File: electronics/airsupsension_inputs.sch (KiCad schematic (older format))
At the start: 46 parts, among them U6 LM324ID, U7 LM324ID

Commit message: more footprints...
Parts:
- C10: value 220nF -> 220n; footprint (none) -> Capacitors_SMD:C_0805; farnell (none) -> 1288261; name (none) -> C0805C224K5RACTU
- C11, C12, C13, C14, C15, C16, C7, C8: footprint (none) -> Capacitors_SMD:C_0805; farnell (none) -> 2118131; name (none) -> C0805C105K5RACTU
- C9: footprint (none) -> Capacitors_SMD:C_0805; farnell (none) -> 1288261; name (none) -> C0805C224K5RACTU
- F1, F2, F3, F4, F5, F6, F7, F8: footprint (none) -> Resistors_SMD:R_1210; farnell (none) -> 1345917; name (none) -> MICROSMD010F-2
- R27, R28, R33, R34, R39, R41, R47, R48: footprint (none) -> Resistors_SMD:R_0805; farnell (none) -> 612522; name (none) -> CR0805-FX-1002ELF
- R29, R31, R35, R37, R42, R44, R49, R51: footprint (none) -> Resistors_SMD:R_0805; farnell (none) -> 2117129; name (none) -> RP73PF2A499RBTDF
- R30, R32, R36, R38, R43, R45, R50, R52: footprint (none) -> Resistors_SMD:R_0805; farnell (none) -> 1577659; name (none) -> ERA6AEB102V
- R40, R46: footprint (none) -> Resistors_SMD:R_0805; farnell (none) -> 1575826; name (none) -> MCTC0525B2001T5E
- U6, U7: value LM324ID -> LM224; footprint (none) -> SMD_Packages:SOIC-14_N; farnell (none) -> 1426352; name (none) -> LM224DR2G
- U6, U7: value LM324ID -> LM224
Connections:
- wire segments 89 -> 88

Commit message: Firmware and some changes in electronics schema
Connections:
- wire segments 88 -> 92
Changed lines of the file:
@@
 $EndComp
 $Comp
-L GND #PWR25
+L GND #PWR022
 U 1 1 5505A367
 P 2450 2750
-F 0 "#PWR25" H 2450 2500 60  0001 C CNN
+F 0 "#PWR022" H 2450 2500 60  0001 C CNN
 F 1 "GND" H 2450 2600 60  0000 C CNN
 F 2 "" H 2450 2750 60  0000 C CNN
@@
 $EndComp
 $Comp
-L GND #PWR21
+L GND #PWR023
 U 1 1 5505A385
 P 1650 2150
-F 0 "#PWR21" H 1650 1900 60  0001 C CNN
+F 0 "#PWR023" H 1650 1900 60  0001 C CNN
 F 1 "GND" H 1650 2000 60  0000 C CNN
 F 2 "" H 1650 2150 60  0000 C CNN
@@
 $EndComp
 $Comp
-L GND #PWR19
+L GND #PWR024
 U 1 1 5505A3C1
 P 1050 2050
-F 0 "#PWR19" H 1050 1800 60  0001 C CNN
+F 0 "#PWR024" H 1050 1800 60  0001 C CNN
 F 1 "GND" H 1050 1900 60  0000 C CNN
 F 2 "" H 1050 2050 60  0000 C CNN
@@
 $EndComp
 $Comp
-L GND #PWR23
+L GND #PWR025
 U 1 1 5505A61E
 P 2150 1350
-F 0 "#PWR23" H 2150 1100 60  0001 C CNN
+F 0 "#PWR025" H 2150 1100 60  0001 C CNN
 F 1 "GND" H 2150 1200 60  0000 C CNN
 F 2 "" H 2150 1350 60  0000 C CNN
@@
 $EndComp
 $Comp
-L GND #PWR26
+L GND #PWR026
 U 1 1 5505C0F9
 P 2550 5750
-F 0 "#PWR26" H 2550 5500 60  0001 C CNN
+F 0 "#PWR026" H 2550 5500 60  0001 C CNN
 F 1 "GND" H 2550 5600 60  0000 C CNN
 F 2 "" H 2550 5750 60  0000 C CNN
@@
 $EndComp
 $Comp
-L GND #PWR22
+L GND #PWR027
 U 1 1 5505C0FF
 P 1750 5150
-F 0 "#PWR22" H 1750 4900 60  0001 C CNN
+F 0 "#PWR027" H 1750 4900 60  0001 C CNN
 F 1 "GND" H 1750 5000 60  0000 C CNN
 F 2 "" H 1750 5150 60  0000 C CNN
@@
 $EndComp
 $Comp
-L GND #PWR20
+L GND #PWR028
 U 1 1 5505C105
 P 1150 5050
-F 0 "#PWR20" H 1150 4800 60  0001 C CNN
+F 0 "#PWR028" H 1150 4800 60  0001 C CNN
 F 1 "GND" H 1150 4900 60  0000 C CNN
 F 2 "" H 1150 5050 60  0000 C CNN
@@
 $EndComp
 $Comp
-L GND #PWR31
+L GND #PWR029
 U 1 1 5505C836
 P 4800 2700
-F 0 "#PWR31" H 4800 2450 60  0001 C CNN
+F 0 "#PWR029" H 4800 2450 60  0001 C CNN
 F 1 "GND" H 4800 2550 60  0000 C CNN
 F 2 "" H 4800 2700 60  0000 C CNN
@@
 $EndComp
 $Comp
-L GND #PWR29
+L GND #PWR030
 U 1 1 5505C83C
 P 4000 2100
-F 0 "#PWR29" H 4000 1850 60  0001 C CNN
+F 0 "#PWR030" H 4000 1850 60  0001 C CNN
 F 1 "GND" H 4000 1950 60  0000 C CNN
 F 2 "" H 4000 2100 60  0000 C CNN
@@
 $EndComp
 $Comp
-L GND #PWR27
+L GND #PWR031
 U 1 1 5505C842
 P 3400 2000
-F 0 "#PWR27" H 3400 1750 60  0001 C CNN
+F 0 "#PWR031" H 3400 1750 60  0001 C CNN
 F 1 "GND" H 3400 1850 60  0000 C CNN
 F 2 "" H 3400 2000 60  0000 C CNN
@@
 $EndComp
 $Comp
-L GND #PWR38
+L GND #PWR032
 U 1 1 5505CD91
 P 7250 2700
-F 0 "#PWR38" H 7250 2450 60  0001 C CNN
+F 0 "#PWR032" H 7250 2450 60  0001 C CNN
 F 1 "GND" H 7250 2550 60  0000 C CNN
 F 2 "" H 7250 2700 60  0000 C CNN
@@
 $EndComp
 $Comp
-L GND #PWR35
+L GND #PWR033
 U 1 1 5505CD97
 P 6450 2100
-F 0 "#PWR35" H 6450 1850 60  0001 C CNN
+F 0 "#PWR033" H 6450 1850 60  0001 C CNN
 F 1 "GND" H 6450 1950 60  0000 C CNN
 F 2 "" H 6450 2100 60  0000 C CNN
@@
 $EndComp
 $Comp
-L GND #PWR33
+L GND #PWR034
 U 1 1 5505CD9D
 P 5850 2000
-F 0 "#PWR33" H 5850 1750 60  0001 C CNN
+F 0 "#PWR034" H 5850 1750 60  0001 C CNN
 F 1 "GND" H 5850 1850 60  0000 C CNN
 F 2 "" H 5850 2000 60  0000 C CNN
@@
 $EndComp
 $Comp
-L GND #PWR44
+L GND #PWR035
 U 1 1 5505D503
 P 10200 2800
-F 0 "#PWR44" H 10200 2550 60  0001 C CNN
+F 0 "#PWR035" H 10200 2550 60  0001 C CNN
 F 1 "GND" H 10200 2650 60  0000 C CNN
 F 2 "" H 10200 2800 60  0000 C CNN
@@
 $EndComp
 $Comp
-L GND #PWR42
+L GND #PWR036
 U 1 1 5505D509
 P 9400 2200
-F 0 "#PWR42" H 9400 1950 60  0001 C CNN
+F 0 "#PWR036" H 9400 1950 60  0001 C CNN
 F 1 "GND" H 9400 2050 60  0000 C CNN
 F 2 "" H 9400 2200 60  0000 C CNN
@@
 $EndComp
 $Comp
-L GND #PWR41
+L GND #PWR037
 U 1 1 5505D50F
 P 8800 2100
-F 0 "#PWR41" H 8800 1850 60  0001 C CNN
+F 0 "#PWR037" H 8800 1850 60  0001 C CNN
 F 1 "GND" H 8800 1950 60  0000 C CNN
 F 2 "" H 8800 2100 60  0000 C CNN
@@
 $EndComp
 $Comp
-L GND #PWR32
+L GND #PWR038
 U 1 1 5505D6E9
 P 5050 5750
-F 0 "#PWR32" H 5050 5500 60  0001 C CNN
+F 0 "#PWR038" H 5050 5500 60  0001 C CNN
 F 1 "GND" H 5050 5600 60  0000 C CNN
 F 2 "" H 5050 5750 60  0000 C CNN
@@
 $EndComp
 $Comp
-L GND #PWR30
+L GND #PWR039
 U 1 1 5505D6EF
 P 4250 5150
-F 0 "#PWR30" H 4250 4900 60  0001 C CNN
+F 0 "#PWR039" H 4250 4900 60  0001 C CNN
 F 1 "GND" H 4250 5000 60  0000 C CNN
 F 2 "" H 4250 5150 60  0000 C CNN
@@
 $EndComp
 $Comp
-L GND #PWR28
+L GND #PWR040
 U 1 1 5505D6F5
 P 3650 5050
-F 0 "#PWR28" H 3650 4800 60  0001 C CNN
+F 0 "#PWR040" H 3650 4800 60  0001 C CNN
 F 1 "GND" H 3650 4900 60  0000 C CNN
 F 2 "" H 3650 5050 60  0000 C CNN
@@
 $EndComp
 $Comp
-L GND #PWR39
+L GND #PWR041
 U 1 1 5505D87C
 P 7600 5850
-F 0 "#PWR39" H 7600 5600 60  0001 C CNN
+F 0 "#PWR041" H 7600 5600 60  0001 C CNN
 F 1 "GND" H 7600 5700 60  0000 C CNN
 F 2 "" H 7600 5850 60  0000 C CNN
@@
 $EndComp
 $Comp
-L GND #PWR36
+L GND #PWR042
 U 1 1 5505D882
 P 6800 5250
-F 0 "#PWR36" H 6800 5000 60  0001 C CNN
+F 0 "#PWR042" H 6800 5000 60  0001 C CNN
 F 1 "GND" H 6800 5100 60  0000 C CNN
 F 2 "" H 6800 5250 60  0000 C CNN
@@
 $EndComp
 $Comp
-L GND #PWR34
+L GND #PWR043
 U 1 1 5505D888
 P 5950 5250
-F 0 "#PWR34" H 5950 5000 60  0001 C CNN
+F 0 "#PWR043" H 5950 5000 60  0001 C CNN
 F 1 "GND" H 5950 5100 60  0000 C CNN
 F 2 "" H 5950 5250 60  0000 C CNN
@@
 Wire Wire Line
 	6400 5550 6400 4950
-Wire Wire Line
-	5950 4750 6400 4750
 Text GLabel 6800 4250 2    60   Input ~ 0
 +5V
@@
 	1    0    0    -1
 $EndComp
-Connection ~ 6200 4750
 Wire Wire Line
 	6200 5150 6200 5250
@@
 $EndComp
 $Comp
-L GND #PWR45
+L GND #PWR044
 U 1 1 5505E94C
 P 10250 5700
-F 0 "#PWR45" H 10250 5450 60  0001 C CNN
+F 0 "#PWR044" H 10250 5450 60  0001 C CNN
 F 1 "GND" H 10250 5550 60  0000 C CNN
 F 2 "" H 10250 5700 60  0000 C CNN
@@
 $EndComp
 $Comp
-L GND #PWR43
+L GND #PWR045
 U 1 1 5505E952
 P 9450 5100
-F 0 "#PWR43" H 9450 4850 60  0001 C CNN
+F 0 "#PWR045" H 9450 4850 60  0001 C CNN
 F 1 "GND" H 9450 4950 60  0000 C CNN
 F 2 "" H 9450 5100 60  0000 C CNN
@@
 $EndComp
 $Comp
-L GND #PWR40
+L GND #PWR046
 U 1 1 5505E958
 P 8600 5100
-F 0 "#PWR40" H 8600 4850 60  0001 C CNN
+F 0 "#PWR046" H 8600 4850 60  0001 C CNN
 F 1 "GND" H 8600 4950 60  0000 C CNN
 F 2 "" H 8600 5100 60  0000 C CNN
@@
 Wire Wire Line
 	9050 5400 9050 4800
-Wire Wire Line
-	8600 4600 9050 4600
 Text GLabel 9450 4100 2    60   Input ~ 0
 +5V
@@
 $EndComp
 $Comp
-L GND #PWR37
+L GND #PWR047
 U 1 1 5511D5C7
 P 6900 1300
-F 0 "#PWR37" H 6900 1050 60  0001 C CNN
+F 0 "#PWR047" H 6900 1050 60  0001 C CNN
 F 1 "GND" H 6900 1150 60  0000 C CNN
 F 2 "" H 6900 1300 60  0000 C CNN
@@
 Wire Wire Line
 	6900 1250 6900 1300
+Wire Wire Line
+	6400 4750 6200 4750
+Wire Wire Line
+	6200 4250 5950 4250
+Wire Wire Line
+	5950 4250 5950 4750
+Wire Wire Line
+	8850 4600 9050 4600
+Wire Wire Line
+	8850 4100 8600 4100
+Wire Wire Line
+	8600 4100 8600 4600
 $EndSCHEMATC

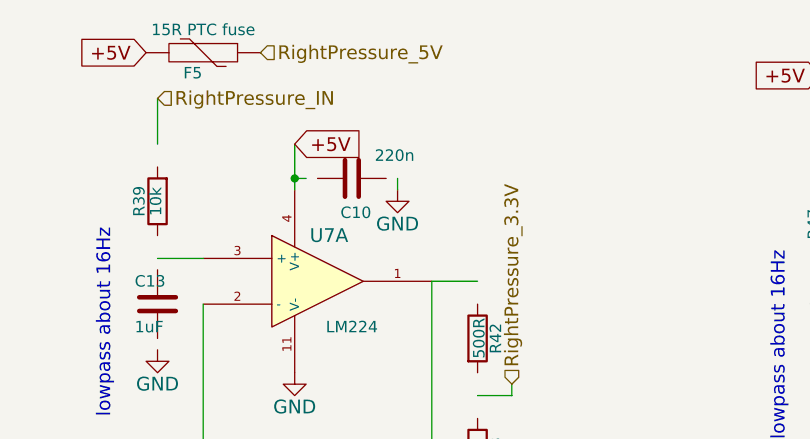
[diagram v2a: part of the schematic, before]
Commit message: Some more footprints and beginning PCB work
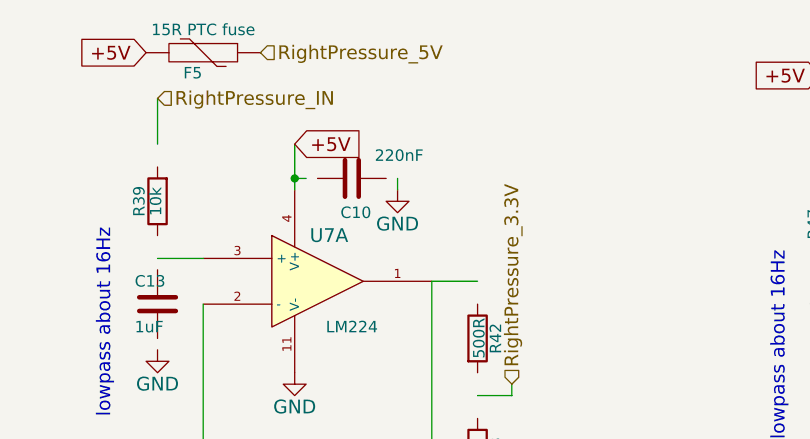
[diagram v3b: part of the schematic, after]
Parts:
- C10: value 220n -> 220nF
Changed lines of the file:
@@
 P 6700 1250
 F 0 "C10" V 6850 1200 50  0000 L CNN
-F 1 "220n" V 6600 1350 50  0000 L CNN
+F 1 "220nF" V 6600 1350 50  0000 L CNN
 F 2 "Capacitors_SMD:C_0805" H 6738 1100 30  0001 C CNN
 F 3 "" H 6700 1250 60  0000 C CNN

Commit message: Changed to a more stable powersupply (3Amps 5V and separate 3.3v) + some few cleanups due to updated kicad
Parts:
- U6, U7: symbol LM324AN -> LM324AN-RESCUE-airsuspension_controller
- U6, U7: footprint (none) -> SMD_Packages:SOIC-14_N; symbol LM324AN -> LM324AN-RESCUE-airsuspension_controller
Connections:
- wire segments 92 -> 133
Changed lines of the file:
@@
 EESchema Schematic File Version 2
+LIBS:airsuspension_controller-rescue
 LIBS:power
 LIBS:device
@@
 LIBS:memory
 LIBS:xilinx
-LIBS:special
 LIBS:microcontrollers
 LIBS:dsp
@@
 Sheet 3 6
 Title ""
-Date ""
+Date "3 aug 2015"
 Rev ""
 Comp ""
@@
 $EndDescr
 $Comp
-L LM324AN U6
+L LM324AN-RESCUE-airsuspension_controller U6
 U 1 1 5505A221
 P 1750 1750
+AR Path="/5505A221" Ref="U6"  Part="1"
+AR Path="/550626C9/5505A221" Ref="U6"  Part="1"
 F 0 "U6" H 1800 1950 60  0000 C CNN
 F 1 "LM224" H 1900 1550 50  0000 C CNN
@@
 +5V
 Wire Wire Line
-	2100 1300 2150 1300
+	2050 1300 2150 1300
 Wire Wire Line
 	2150 1300 2150 1350
 Wire Wire Line
-	1700 1300 1650 1300
+	1650 1300 1750 1300
 Connection ~ 1650 1300
 Wire Wire Line
-	1050 950  1050 1150
-$Comp
-L LM324AN U6
+	1050 950  1050 1250
+$Comp
+L LM324AN-RESCUE-airsuspension_controller U6
 U 2 1 5505C0DB
 P 1850 4750
+AR Path="/5505C0DB" Ref="U6"  Part="2"
+AR Path="/550626C9/5505C0DB" Ref="U6"  Part="2"
 F 0 "U6" H 1900 4950 60  0000 C CNN
 F 1 "LM224" H 2000 4550 50  0000 C CNN
-F 2 "" H 1850 4750 60  0001 C CNN
+F 2 "SMD_Packages:SOIC-14_N" H 1850 4750 60  0001 C CNN
 F 3 "" H 1850 4750 60  0000 C CNN
 	2    1850 4750
@@
 +5V
 Wire Wire Line
-	1150 3950 1150 4150
+	1150 3950 1150 4250
 $Comp
 L C C11
@@
 +5V
 Wire Wire Line
-	3400 900  3400 1100
-$Comp
-L LM324AN U6
+	3400 900  3400 1200
+$Comp
+L LM324AN-RESCUE-airsuspension_controller U6
 U 3 1 5505C818
 P 4100 1700
+AR Path="/5505C818" Ref="U6"  Part="3"
+AR Path="/550626C9/5505C818" Ref="U6"  Part="3"
 F 0 "U6" H 4150 1900 60  0000 C CNN
 F 1 "LM224" H 4250 1500 50  0000 C CNN
-F 2 "" H 4100 1700 60  0001 C CNN
+F 2 "SMD_Packages:SOIC-14_N" H 4100 1700 60  0001 C CNN
 F 3 "" H 4100 1700 60  0000 C CNN
 	3    4100 1700
@@
 +5V
 Wire Wire Line
-	5850 900  5850 1100
-$Comp
-L LM324AN U7
+	5850 900  5850 1200
+$Comp
+L LM324AN-RESCUE-airsuspension_controller U7
 U 1 1 5505CDB8
 P 6550 1700
+AR Path="/5505CDB8" Ref="U7"  Part="1"
+AR Path="/550626C9/5505CDB8" Ref="U7"  Part="1"
 F 0 "U7" H 6600 1900 60  0000 C CNN
 F 1 "LM224" H 6700 1500 50  0000 C CNN
@@
 +5V
 Wire Wire Line
-	8800 1000 8800 1200
-$Comp
-L LM324AN U7
+	8800 1000 8800 1300
+$Comp
+L LM324AN-RESCUE-airsuspension_controller U7
 U 3 1 5505D52A
 P 9500 1800
+AR Path="/5505D52A" Ref="U7"  Part="3"
+AR Path="/550626C9/5505D52A" Ref="U7"  Part="3"
 F 0 "U7" H 9550 2000 60  0000 C CNN
 F 1 "LM224" H 9650 1600 50  0000 C CNN
-F 2 "" H 9500 1800 60  0001 C CNN
+F 2 "SMD_Packages:SOIC-14_N" H 9500 1800 60  0001 C CNN
 F 3 "" H 9500 1800 60  0000 C CNN
 	3    9500 1800
@@
 +5V
 Wire Wire Line
-	3650 3950 3650 4150
-$Comp
-L LM324AN U6
+	3650 3950 3650 4250
+$Comp
+L LM324AN-RESCUE-airsuspension_controller U6
 U 4 1 5505D710
 P 4350 4750
+AR Path="/5505D710" Ref="U6"  Part="4"
+AR Path="/550626C9/5505D710" Ref="U6"  Part="4"
 F 0 "U6" H 4400 4950 60  0000 C CNN
 F 1 "LM224" H 4500 4550 50  0000 C CNN
-F 2 "" H 4350 4750 60  0001 C CNN
+F 2 "SMD_Packages:SOIC-14_N" H 4350 4750 60  0001 C CNN
 F 3 "" H 4350 4750 60  0000 C CNN
 	4    4350 4750
@@
 +5V
 Wire Wire Line
-	6200 4050 6200 4250
-$Comp
-L LM324AN U7
+	6200 4050 6200 4350
+$Comp
+L LM324AN-RESCUE-airsuspension_controller U7
 U 2 1 5505D8A3
 P 6900 4850
+AR Path="/5505D8A3" Ref="U7"  Part="2"
+AR Path="/550626C9/5505D8A3" Ref="U7"  Part="2"
 F 0 "U7" H 6950 5050 60  0000 C CNN
 F 1 "LM224" H 7050 4650 50  0000 C CNN
-F 2 "" H 6900 4850 60  0001 C CNN
+F 2 "SMD_Packages:SOIC-14_N" H 6900 4850 60  0001 C CNN
 F 3 "" H 6900 4850 60  0000 C CNN
 	2    6900 4850
@@
 $EndComp
 Wire Wire Line
-	6200 5150 6200 5250
+	6200 5100 6200 5250
 Wire Wire Line
 	6200 5250 5950 5250
@@
 +5V
 Wire Wire Line
-	8850 3900 8850 4100
-$Comp
-L LM324AN U7
+	8850 3900 8850 4200
+$Comp
+L LM324AN-RESCUE-airsuspension_controller U7
 U 4 1 5505E972
 P 9550 4700
+AR Path="/5505E972" Ref="U7"  Part="4"
+AR Path="/550626C9/5505E972" Ref="U7"  Part="4"
 F 0 "U7" H 9600 4900 60  0000 C CNN
 F 1 "LM224" H 9700 4500 50  0000 C CNN
-F 2 "" H 9550 4700 60  0001 C CNN
+F 2 "SMD_Packages:SOIC-14_N" H 9550 4700 60  0001 C CNN
 F 3 "" H 9550 4700 60  0000 C CNN
 	4    9550 4700
@@
 Connection ~ 8850 4600
 Wire Wire Line
-	8850 5000 8850 5100
+	8850 4950 8850 5100
 Wire Wire Line
 	8850 5100 8600 5100
@@
 $EndComp
 Wire Wire Line
-	6500 1250 6450 1250
+	6450 1250 6550 1250
 Connection ~ 6450 1250
 Wire Wire Line
@@
 	6200 4250 5950 4250
 Wire Wire Line
-	5950 4250 5950 4750
+	5950 4250 5950 4850
 Wire Wire Line
 	8850 4600 9050 4600
@@
 	8850 4100 8600 4100
 Wire Wire Line
-	8600 4100 8600 4600
+	8600 4100 8600 4700
+Wire Wire Line
+	1050 1550 1050 1700
+Connection ~ 1050 1650
+Wire Wire Line
+	1050 2000 1050 2050
+Wire Wire Line
+	2450 1750 2450 1850
+Wire Wire Line
+	2450 2150 2450 2350
+Connection ~ 2450 2250
+Wire Wire Line
+	2450 2750 2450 2650
+Wire Wire Line
+	3400 1500 3400 1650
+Connection ~ 3400 1600
+Wire Wire Line
+	4800 1700 4800 1800
+Wire Wire Line
+	4800 2100 4800 2300
+Connection ~ 4800 2200
+Wire Wire Line
+	4800 2600 4800 2700
+Wire Wire Line
+	1150 4550 1150 4700
+Connection ~ 1150 4650
+Wire Wire Line
+	1150 5000 1150 5050
+Wire Wire Line
+	2550 4750 2550 4850
+Wire Wire Line
+	2550 5150 2550 5350
+Connection ~ 2550 5250
+Wire Wire Line
+	2550 5650 2550 5750
+Wire Wire Line
+	5050 5650 5050 5750
+Wire Wire Line
+	5050 5150 5050 5350
+Connection ~ 5050 5250
+Wire Wire Line
+	5050 4750 5050 4850
+Wire Wire Line
+	3650 4550 3650 4700
+Connection ~ 3650 4650
+Wire Wire Line
+	6200 4650 6200 4800
+Connection ~ 6200 4750
+Wire Wire Line
+	5950 5250 5950 5150
+Wire Wire Line
+	8600 5100 8600 5000
+Wire Wire Line
+	8850 4500 8850 4650
+Connection ~ 8850 4100
+Connection ~ 6200 4250
+Wire Wire Line
+	7600 4850 7600 4950
+Wire Wire Line
+	7600 5250 7600 5450
+Connection ~ 7600 5350
+Wire Wire Line
+	7600 5750 7600 5850
+Wire Wire Line
+	10250 4700 10250 4800
+Wire Wire Line
+	10250 5100 10250 5300
+Connection ~ 10250 5200
+Wire Wire Line
+	10250 5600 10250 5700
+Wire Wire Line
+	8800 1600 8800 1750
+Connection ~ 8800 1700
+Wire Wire Line
+	8800 2050 8800 2100
+Wire Wire Line
+	10200 1800 10200 1900
+Wire Wire Line
+	10200 2200 10200 2400
+Connection ~ 10200 2300
+Wire Wire Line
+	10200 2700 10200 2800
+Wire Wire Line
+	7250 1700 7250 1800
+Wire Wire Line
+	7250 2100 7250 2300
+Connection ~ 7250 2200
+Wire Wire Line
+	7250 2600 7250 2700
+Wire Wire Line
+	5850 1950 5850 2000
+Wire Wire Line
+	5850 1500 5850 1650
+Connection ~ 5850 1600
+Wire Wire Line
+	6900 1250 6850 1250
+Wire Wire Line
+	3400 1950 3400 2000
+Wire Wire Line
+	3650 5000 3650 5050
 $EndSCHEMATC

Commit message: Some updates as some parts were not available
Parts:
- C10, C9: name C0805C224K5RACTU -> (none); part (none) -> C0805C224K5RACTU
- C11, C12, C13, C14, C15, C16, C7, C8: name C0805C105K5RACTU -> (none); part (none) -> C0805C105K5RACTU
- F1, F2, F3, F4, F5, F6, F7, F8: name MICROSMD010F-2 -> (none); part (none) -> MICROSMD010F-2
- R27, R28, R33, R34, R39, R41, R47, R48: farnell 612522 -> 9332391; name CR0805-FX-1002ELF -> (none)
- R29, R31, R35, R37, R42, R44, R49, R51: farnell 2117129 -> 1469936; name RP73PF2A499RBTDF -> (none)
- R30, R32, R36, R38, R43, R45, R50, R52: farnell 1577659 -> 9332383; name ERA6AEB102V -> (none)
- R40, R46: farnell 1575826 -> 9332766; name MCTC0525B2001T5E -> (none)
- U6, U7: name LM224DR2G -> (none); part (none) -> LM224DR2G
